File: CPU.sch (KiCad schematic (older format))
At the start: 1 part, among them P55 9S12XDP512

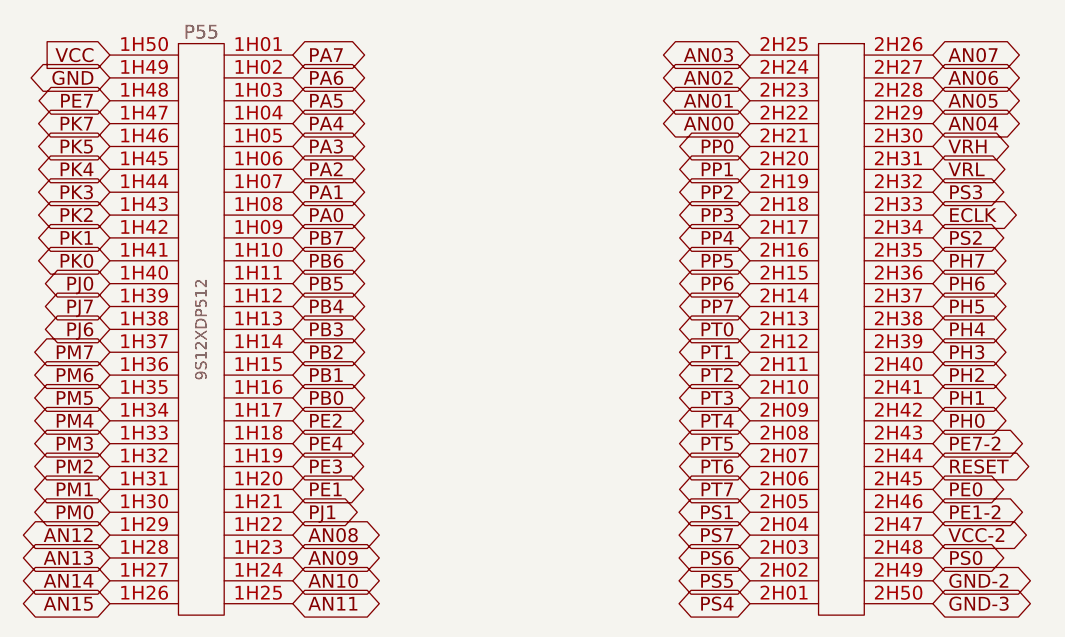
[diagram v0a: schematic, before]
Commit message: Removed LM1815 options. Now adaptive mode and square waves are the default,
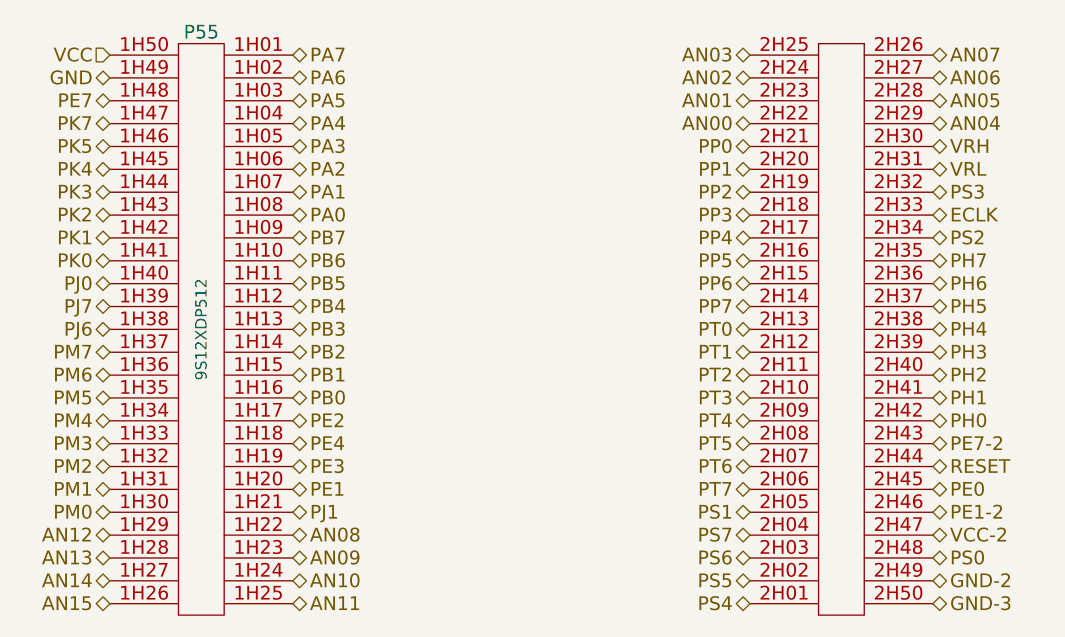
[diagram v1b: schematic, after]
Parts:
- P55: Field1 (none) -> vendor1, thru w hem; Field2 (none) -> vendor1, smd w hem; Field3 (none) -> vendor2, thru w hem; Field4 (none) -> vendor2, smd w hem; Field5 (none) -> x,x; Field6 (none) -> x,x; Field7 (none) -> x; Field8 (none) -> other,more,stuff

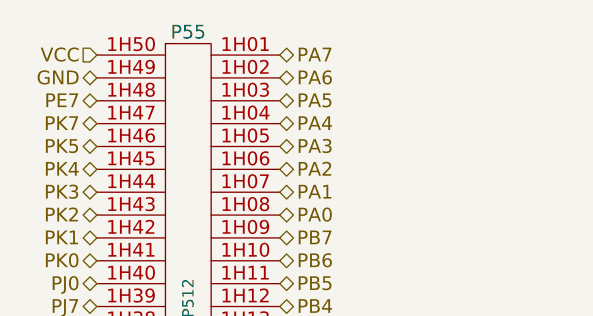
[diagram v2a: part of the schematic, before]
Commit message: Implemented P&H, removed current sense circuitry, removed all unnecessary files from the repo
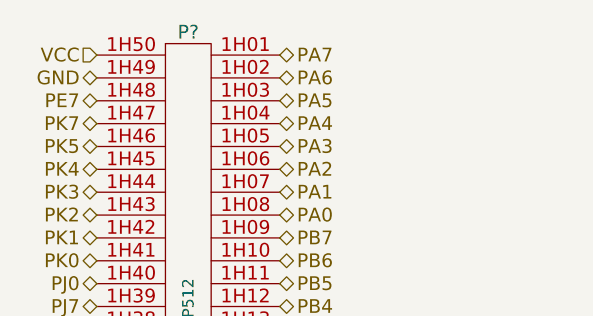
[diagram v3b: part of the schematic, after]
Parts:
- renumbered P55 to P?
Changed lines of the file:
@@
-EESchema Schematic File Version 2  date Fri 02 Jul 2010 05:44:26 PM ART
+EESchema Schematic File Version 2  date Sat 03 Jul 2010 10:49:02 AM ART
 LIBS:power
 LIBS:freeEMS_lib
@@
 EELAYER END
 $Descr A 11000 8500
-Sheet 41 41
+Sheet 43 41
 Title "freeEMS 1.0"
-Date "2 jul 2010"
-Rev "A.20"
+Date "3 jul 2010"
+Rev "A.08"
 Comp "diyefi.org"
 Comment1 ""
@@
 $EndDescr
 $Comp
-L 9S12XDP512 P55
+L 9S12XDP512 P?
 U 1 1 4893CC4C
 P 3300 3800
-F 0 "P55" H 3300 5100 60  0000 C CNN
+F 0 "P?" H 3300 5100 60  0000 C CNN
 F 1 "9S12XDP512" V 3300 3800 50  0000 C CNN
 F 2 "9S12XDP512" V 4080 5550 60  0001 C CNN

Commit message: Corrected ERC errors by fixing the custom FreeEMS components pinouts
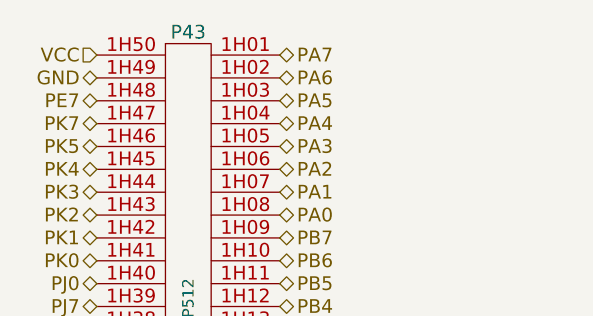
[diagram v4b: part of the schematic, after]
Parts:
- gave numbers to parts that had none: 1
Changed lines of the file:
@@
-EESchema Schematic File Version 2  date Sat 03 Jul 2010 10:49:02 AM ART
+EESchema Schematic File Version 2  date Sat 03 Jul 2010 12:32:24 PM ART
 LIBS:power
 LIBS:freeEMS_lib
@@
 $EndDescr
 $Comp
-L 9S12XDP512 P?
+L 9S12XDP512 P43
 U 1 1 4893CC4C
 P 3300 3800
-F 0 "P?" H 3300 5100 60  0000 C CNN
+F 0 "P43" H 3300 5100 60  0000 C CNN
 F 1 "9S12XDP512" V 3300 3800 50  0000 C CNN
 F 2 "9S12XDP512" V 4080 5550 60  0001 C CNN
